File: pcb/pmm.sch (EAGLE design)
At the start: 12 parts, among them IC2 REG1117, IC3 STM32F042F4, U2 USBC_16P

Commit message: pcb done
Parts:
- removed JP15, JPAE: (no value), pinhead:PINHD-1X5
- added C3, C5: 10uF, clock:CAP0805
- added C4: 100nF, clock:CAP0805
- added LED1, LED2: (no value), adafruit:LEDCHIP-LED0805
- added R3, R5: 10K, joyAnalog:RESISTOR0805-RES
- added R4, R7: 2K, SparkFun-Passives:RESISTOR0805-RES
- added SW3, SW4: 324_SW, 3pos_slide_switch_centered:324_SW
- added U$3, U$4, U$5, U$6: PINHD5, adafruit_changed:PINHD5
- C1: value 100nF -> 10uF
- JP1: device pinhead:PINHD-1X6 -> adafruit:PINHD-1X6CB
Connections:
- removed net DNDNDN: U2.DN1, U2.DN2
- new net +5V: C1.2, C3.2, C5.2, IC2.VIN, JP1.5, R3.2, U$1G$1.RESET_N, U$1G$1.VDD, U$2G$1.RESET_N, U$2G$1.VDD, U$5.4, U2.VBUS
- new net BUTTON1: IC3.NRST, SW3.2, SW3.3
- new net BUTTON2: IC3.BOOT0/PB8, R5.2, SW4.2, SW4.3
- new net N$10: IC3.PA1, JP1.3
- new net N$11: IC3.PA0, JP1.4
- new net N$12: IC3.PF0/OSC_IN, U$5.2
- new net N$13: IC3.PF1/OSC_OUT, U$5.3
- new net N$2: IC3.PA7, U$1G$1.DIN
- new net N$29: LED2.C, R7.2
- new net N$3: U$1G$1.DOUT, U$2G$1.DIN
- new net N$4: IC3.PB1, R3.1, U$1G$1.SYNC_N, U$2G$1.SYNC_N
- new net N$5: LED1.C, R4.2
- new net N$6: IC3.PA2, U$6.3
- new net N$7: IC3.PA14, U$6.1
- new net N$8: IC3.PA13, U$6.2
- new net N$9: IC3.PA3, JP1.2
- new net USB_DN: IC3.PA9/PA11, U2.DN1, U2.DN2
- new net USER_LED: IC3.PA4, R4.1
- net +3V3: now also C4.2, IC3.VDD, IC3.VDDA, JP1.6, LED1.A, LED2.A, SW4.1, SW4.4, U$5.5, U$6.4; no longer JP1.4
- net 1: now also U$3.1; no longer JP15.1
- net 2: now also U$3.2; no longer JP15.2
- net 3: now also U$3.3; no longer JP15.3
- net 4: now also U$3.4; no longer JP15.4
- net 5: now also U$3.5; no longer JP15.5
- net A: now also U$4.1; no longer JPAE.1
- net B: now also U$4.2; no longer JPAE.2
- net C: now also U$4.3; no longer JPAE.3
- net E: now also U$4.5; no longer JPAE.5
- net GND: now also C3.1, C4.1, C5.1, IC3.VSS, JP1.1, R5.1, R7.1, SW3.1, SW3.4, U$1G$1.GND, U$1G$1.VSS, U$2G$1.GND, U$2G$1.VSS, U$5.1, U$6.5; no longer JP1.5
- net N$1: now also IC3.PA5, U$1G$1.SCLK, U$2G$1.SCLK; no longer C1.2, IC2.VIN, U2.VBUS
- net USB_DP: now also IC3.PA10/PA12
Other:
- note added: "SW_1 SW_2 SW_3"
- note added: "SW_4 SW_5 SW_6 SW_STOP SW_START"
- note added: "SW_7 SW_8 SW_9 SW_0"
- note added: "SW_POWER SW_TIME"
- moved on the sheet: IC3, JP1

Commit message: minor cleanup
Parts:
- renumbered R7 to R6
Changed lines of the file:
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@@
 <part name="+3V16" library="backplane" deviceset="+3V3" device=""/>
 <part name="LED2" library="adafruit" deviceset="LED" device="CHIP-LED0805"/>
-<part name="R7" library="SparkFun-Passives" deviceset="RESISTOR" device="0805-RES" value="2K"/>
+<part name="R6" library="SparkFun-Passives" deviceset="RESISTOR" device="0805-RES" value="2K"/>
 <part name="GND9" library="backplane" deviceset="GND" device=""/>
 <part name="+3V2" library="supply1" library_urn="urn:adsk.eagle:library:371" deviceset="+3V3" device=""/>
@@
 <attribute name="VALUE" x="113.792" y="76.835" size="1.778" layer="96" rot="R180"/>
 </instance>
-<instance part="R7" gate="G$1" x="119.38" y="71.12" smashed="yes" rot="R180">
+<instance part="R6" gate="G$1" x="119.38" y="71.12" smashed="yes" rot="R180">
 <attribute name="NAME" x="123.19" y="69.6214" size="1.778" layer="95" rot="R180"/>
 <attribute name="VALUE" x="123.19" y="74.422" size="1.778" layer="96" rot="R180"/>
@@
 </segment>
 <segment>
-<pinref part="R7" gate="G$1" pin="1"/>
+<pinref part="R6" gate="G$1" pin="1"/>
 <pinref part="GND9" gate="1" pin="GND"/>
 </segment>
@@
 <segment>
 <pinref part="LED2" gate="G$1" pin="C"/>
-<pinref part="R7" gate="G$1" pin="2"/>
-</segment>
-</net>
+<pinref part="R6" gate="G$1" pin="2"/>
+</segment>
+</net>

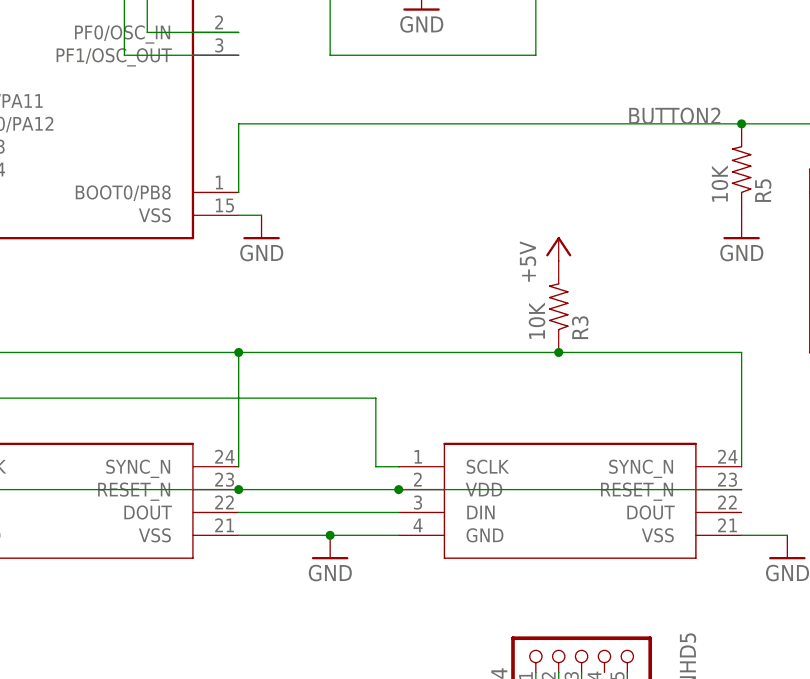
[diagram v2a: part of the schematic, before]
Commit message: added a required pullup resistor
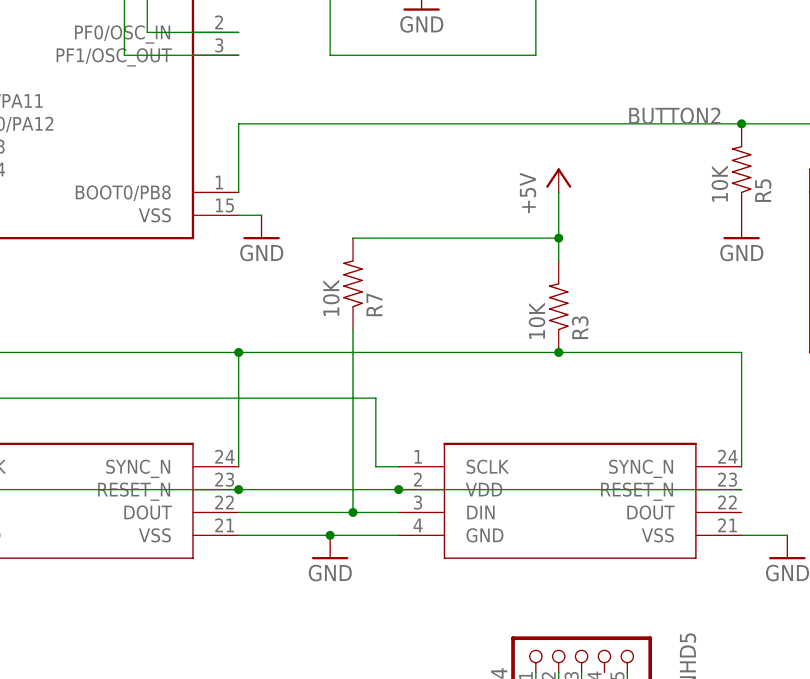
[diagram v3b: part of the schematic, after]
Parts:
- added R7: 10K, joyAnalog:RESISTOR0805-RES
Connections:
- net +5V: now also R7.2
- net N$3: now also R7.1
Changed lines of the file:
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@@
 <part name="GND14" library="supply1" library_urn="urn:adsk.eagle:library:371" deviceset="GND" device=""/>
 <part name="GND15" library="supply1" library_urn="urn:adsk.eagle:library:371" deviceset="GND" device=""/>
+<part name="R7" library="joyAnalog" deviceset="RESISTOR" device="0805-RES" value="10K"/>
 </parts>
 <sheets>
@@
 <attribute name="VALUE" x="52.578" y="-6.35" size="1.778" layer="96" rot="MR90"/>
 </instance>
-<instance part="P+3" gate="1" x="55.88" y="5.08" smashed="yes">
-<attribute name="VALUE" x="53.34" y="0" size="1.778" layer="96" rot="R90"/>
+<instance part="P+3" gate="1" x="55.88" y="12.7" smashed="yes">
+<attribute name="VALUE" x="53.34" y="7.62" size="1.778" layer="96" rot="R90"/>
 </instance>
 <instance part="+3V1" gate="G$1" x="22.86" y="45.72" smashed="yes" rot="MR0">
@@
 <instance part="GND15" gate="1" x="88.9" y="111.76" smashed="yes">
 <attribute name="VALUE" x="86.36" y="109.22" size="1.778" layer="96"/>
+</instance>
+<instance part="R7" gate="G$1" x="33.02" y="0" smashed="yes" rot="MR90">
+<attribute name="NAME" x="34.5186" y="-3.81" size="1.778" layer="95" rot="MR90"/>
+<attribute name="VALUE" x="29.718" y="-3.81" size="1.778" layer="96" rot="MR90"/>
+<attribute name="NAME" x="34.5186" y="-3.81" size="1.778" layer="95" rot="MR90"/>
+<attribute name="VALUE" x="29.718" y="-3.81" size="1.778" layer="96" rot="MR90"/>
 </instance>
 </instances>
@@
 <pinref part="R3" gate="G$1" pin="2"/>
 <pinref part="P+3" gate="1" pin="+5V"/>
+<wire x1="55.88" y1="10.16" x2="55.88" y2="5.08" width="0.1524" layer="91"/>
+<pinref part="R7" gate="G$1" pin="2"/>
+<wire x1="55.88" y1="5.08" x2="55.88" y2="2.54" width="0.1524" layer="91"/>
+<wire x1="33.02" y1="5.08" x2="55.88" y2="5.08" width="0.1524" layer="91"/>
+<junction x="55.88" y="5.08"/>
 </segment>
 <segment>
@@
 <pinref part="U$1" gate="G$1" pin="DOUT"/>
 <pinref part="U$2" gate="G$1" pin="DIN"/>
-<wire x1="20.32" y1="-25.4" x2="38.1" y2="-25.4" width="0.1524" layer="91"/>
-</segment>
-</net>
+<wire x1="20.32" y1="-25.4" x2="33.02" y2="-25.4" width="0.1524" layer="91"/>
+<pinref part="R7" gate="G$1" pin="1"/>
+<wire x1="33.02" y1="-25.4" x2="38.1" y2="-25.4" width="0.1524" layer="91"/>
+<wire x1="33.02" y1="-5.08" x2="33.02" y2="-25.4" width="0.1524" layer="91"/>
+<junction x="33.02" y="-25.4"/>
+</segment>
+</net>
